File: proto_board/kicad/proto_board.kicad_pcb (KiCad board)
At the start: 2 copper layers, 91 x 96 mm, 1067 parts, among them J1 pcie_98

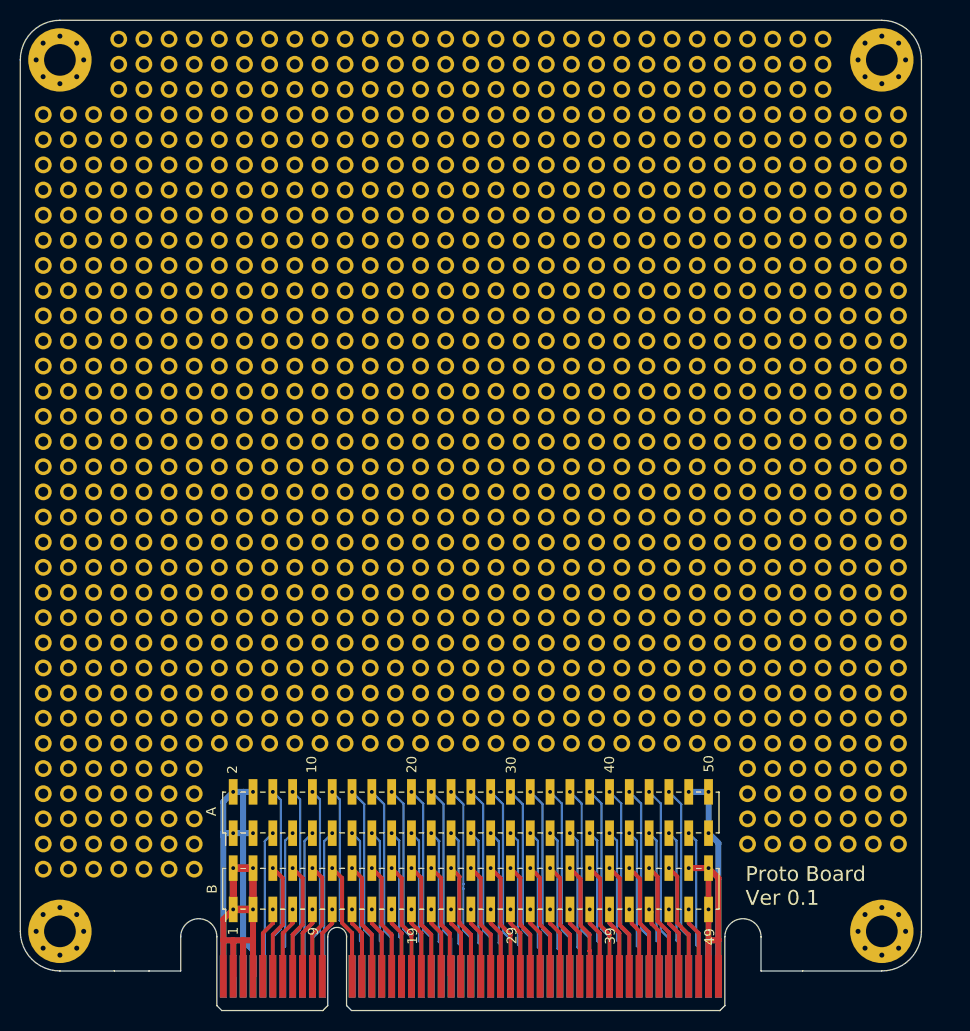
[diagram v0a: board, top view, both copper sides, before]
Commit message: Updated proto board to the common card outline.
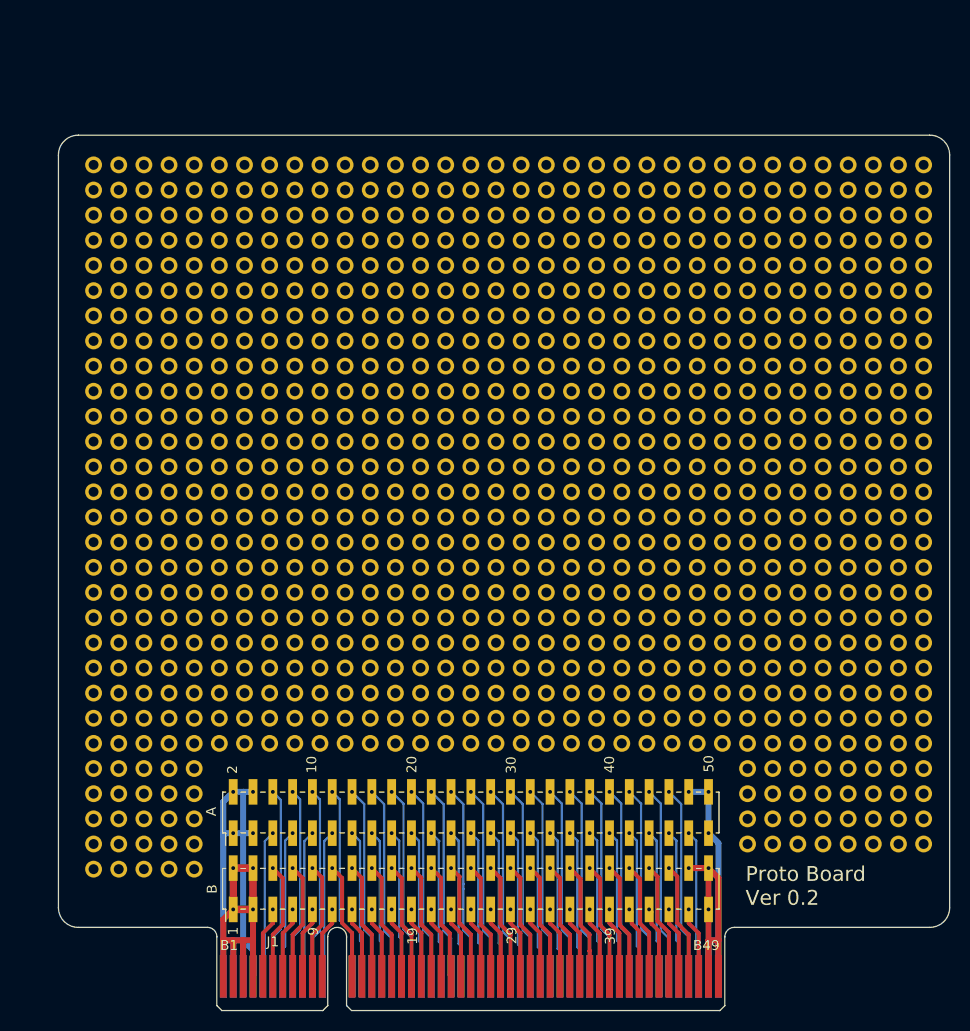
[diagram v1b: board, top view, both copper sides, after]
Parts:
- removed H1, H2, H3, H4: MountingHole, MountingHole:MountingHole_3.2mm_M3_Pad_Via
- removed the REF** at (51.6, -90.5)
- removed the REF** at (-14.4, -95.6)
- removed the REF** at (-14.4, -93.0)
- removed the REF** at (-27.1, -29.5)
- removed the REF** at (33.8, -93.0)
- removed the REF** at (21.1, -87.9)
- removed the REF** at (-27.1, -19.4)
- removed the REF** at (36.4, -90.5)
- removed the REF** at (-29.7, -21.9)
- removed the REF** at (-27.1, -37.1)
- removed the REF** at (5.88, -87.9)
- removed the REF** at (-27.1, -85.4)
- removed the REF** at (-24.6, -87.9)
- removed the REF** at (-29.7, -65.1)
- removed the REF** at (-27.1, -72.7)
- removed the REF** at (-27.1, -77.8)
- removed the REF** at (-29.7, -52.4)
- removed the REF** at (-14.4, -90.5)
- removed the REF** at (46.5, -95.6)
- removed the REF** at (13.5, -98.1)
- removed the REF** at (0.80, -90.5)
- removed the REF** at (49.1, -93.0)
- removed the REF** at (-17.0, -87.9)
- removed the REF** at (-22.1, -98.1)
- removed the REF** at (-29.7, -44.8)
- removed the REF** at (33.8, -90.5)
- removed the REF** at (3.34, -87.9)
- removed the REF** at (49.1, -95.6)
- removed the REF** at (44.0, -93.0)
- removed the REF** at (16.0, -93.0)
- removed the REF** at (-29.7, -14.3)
- removed the REF** at (-27.1, -57.5)
- removed the REF** at (11.0, -87.9)
- removed the REF** at (0.80, -98.1)
- removed the REF** at (-29.7, -60.0)
- removed the REF** at (36.4, -98.1)
- removed the REF** at (28.7, -93.0)
- removed the REF** at (-27.1, -39.7)
- removed the REF** at (-19.5, -98.1)
- removed the REF** at (36.4, -95.6)
- removed the REF** at (-29.7, -34.6)
- removed the REF** at (-9.36, -93.0)
- removed the REF** at (46.5, -87.9)
- removed the REF** at (21.1, -93.0)
- removed the REF** at (-6.82, -93.0)
- removed the REF** at (54.1, -90.5)
- removed the REF** at (11.0, -98.1)
- removed the REF** at (38.9, -95.6)
- removed the REF** at (8.42, -93.0)
- removed the REF** at (28.7, -95.6)
- removed the REF** at (-11.9, -98.1)
- removed the REF** at (38.9, -87.9)
- removed the REF** at (21.1, -98.1)
- removed the REF** at (-14.4, -98.1)
- removed the REF** at (18.6, -90.5)
- removed the REF** at (31.3, -87.9)
- removed the REF** at (-27.1, -24.4)
- removed the REF** at (26.2, -95.6)
- removed the REF** at (28.7, -87.9)
- removed the REF** at (-27.1, -44.8)
- removed the REF** at (0.80, -95.6)
- removed the REF** at (-22.1, -93.0)
- removed the REF** at (-17.0, -90.5)
- removed the REF** at (-29.7, -57.5)
- removed the REF** at (-29.7, -75.2)
- removed the REF** at (-1.74, -87.9)
- removed the REF** at (-29.7, -16.8)
- removed the REF** at (38.9, -93.0)
- removed the REF** at (49.1, -90.5)
- removed the REF** at (-19.5, -95.6)
- removed the REF** at (26.2, -90.5)
- removed the REF** at (-14.4, -87.9)
- removed the REF** at (8.42, -87.9)
- removed the REF** at (-9.36, -95.6)
- removed the REF** at (-27.1, -21.9)
- removed the REF** at (-29.7, -90.5)
- removed the REF** at (-27.1, -49.8)
- removed the REF** at (-27.1, -70.2)
- removed the REF** at (-27.1, -60.0)
- removed the REF** at (-29.7, -80.3)
- removed the REF** at (46.5, -90.5)
- removed the REF** at (33.8, -98.1)
- removed the REF** at (38.9, -98.1)
- removed the REF** at (-4.28, -95.6)
- removed the REF** at (-29.7, -24.4)
- removed the REF** at (16.0, -90.5)
- removed the REF** at (-29.7, -47.3)
- removed the REF** at (18.6, -93.0)
- removed the REF** at (0.80, -93.0)
- removed the REF** at (41.4, -98.1)
- removed the REF** at (8.42, -95.6)
- removed the REF** at (0.80, -87.9)
- removed the REF** at (-29.7, -49.8)
- removed the REF** at (-4.28, -93.0)
- removed the REF** at (5.88, -95.6)
- removed the REF** at (44.0, -90.5)
- removed the REF** at (41.4, -90.5)
- removed the REF** at (-29.7, -62.5)
- removed the REF** at (-17.0, -93.0)
- removed the REF** at (-29.7, -82.9)
- removed the REF** at (21.1, -95.6)
- removed the REF** at (13.5, -87.9)
- removed the REF** at (-27.1, -80.3)
- removed the REF** at (-22.1, -87.9)
- removed the REF** at (13.5, -90.5)
- removed the REF** at (16.0, -98.1)
- removed the REF** at (13.5, -95.6)
- removed the REF** at (-6.82, -87.9)
- removed the REF** at (-1.74, -95.6)
- removed the REF** at (51.6, -87.9)
- removed the REF** at (23.7, -98.1)
- removed the REF** at (23.7, -90.5)
- removed the REF** at (5.88, -90.5)
- removed the REF** at (23.7, -87.9)
- removed the REF** at (16.0, -95.6)
- removed the REF** at (-22.1, -90.5)
- removed the REF** at (-27.1, -87.9)
- removed the REF** at (13.5, -93.0)
- removed the REF** at (18.6, -95.6)
- removed the REF** at (-27.1, -82.9)
- removed the REF** at (-11.9, -87.9)
- removed the REF** at (-27.1, -47.3)
- removed the REF** at (-4.28, -90.5)
- removed the REF** at (49.1, -98.1)
- removed the REF** at (-27.1, -75.2)
- removed the REF** at (-6.82, -95.6)
- removed the REF** at (28.7, -90.5)
- removed the REF** at (44.0, -95.6)
- removed the REF** at (-1.74, -98.1)
- removed the REF** at (-6.82, -90.5)
- removed the REF** at (-29.7, -42.2)
- removed the REF** at (-29.7, -19.4)
- removed the REF** at (-9.36, -98.1)
- removed the REF** at (-27.1, -62.5)
- removed the REF** at (46.5, -98.1)
- removed the REF** at (-17.0, -98.1)
- removed the REF** at (41.4, -95.6)
- removed the REF** at (-11.9, -95.6)
- removed the REF** at (-29.7, -70.2)
- removed the REF** at (31.3, -93.0)
- removed the REF** at (-22.1, -95.6)
- removed the REF** at (41.4, -87.9)
- removed the REF** at (-9.36, -87.9)
- removed the REF** at (-27.1, -42.2)
- removed the REF** at (-4.28, -98.1)
- removed the REF** at (-1.74, -93.0)
- removed the REF** at (-27.1, -67.6)
- removed the REF** at (33.8, -87.9)
- removed the REF** at (18.6, -98.1)
- removed the REF** at (-27.1, -54.9)
- removed the REF** at (26.2, -98.1)
- removed the REF** at (36.4, -93.0)
- removed the REF** at (3.34, -95.6)
- removed the REF** at (56.7, -87.9)
- removed the REF** at (44.0, -87.9)
- removed the REF** at (44.0, -98.1)
- removed the REF** at (31.3, -95.6)
- removed the REF** at (56.7, -90.5)
- removed the REF** at (21.1, -90.5)
- removed the REF** at (16.0, -87.9)
- removed the REF** at (-17.0, -95.6)
- removed the REF** at (-29.7, -77.8)
- removed the REF** at (11.0, -93.0)
- removed the REF** at (11.0, -90.5)
- removed the REF** at (-11.9, -93.0)
- removed the REF** at (8.42, -98.1)
- removed the REF** at (54.1, -87.9)
- removed the REF** at (-27.1, -90.5)
- removed the REF** at (5.88, -98.1)
- removed the REF** at (41.4, -93.0)
- removed the REF** at (-29.7, -72.7)
- removed the REF** at (-6.82, -98.1)
- removed the REF** at (46.5, -93.0)
- removed the REF** at (-1.74, -90.5)
- removed the REF** at (-27.1, -14.3)
- removed the REF** at (-29.7, -37.1)
- removed the REF** at (-29.7, -39.7)
- removed the REF** at (11.0, -95.6)
- removed the REF** at (-29.7, -32.1)
- removed the REF** at (23.7, -93.0)
- removed the REF** at (28.7, -98.1)
- removed the REF** at (-29.7, -29.5)
- removed the REF** at (33.8, -95.6)
- removed the REF** at (-29.7, -67.6)
- removed the REF** at (5.88, -93.0)
- removed the REF** at (-27.1, -32.1)
- removed the REF** at (8.42, -90.5)
- removed the REF** at (38.9, -90.5)
- removed the REF** at (-27.1, -34.6)
- removed the REF** at (26.2, -87.9)
- removed the REF** at (-29.7, -87.9)
- removed the REF** at (-29.7, -54.9)
- removed the REF** at (26.2, -93.0)
- removed the REF** at (18.6, -87.9)
- removed the REF** at (-29.7, -85.4)
- removed the REF** at (-27.1, -27.0)
- removed the REF** at (-27.1, -65.1)
- removed the REF** at (31.3, -98.1)
- removed the REF** at (3.34, -90.5)
- removed the REF** at (-27.1, -52.4)
- removed the REF** at (-27.1, -16.8)
- removed the REF** at (-19.5, -93.0)
- removed the REF** at (49.1, -87.9)
- removed the REF** at (-19.5, -90.5)
- removed the REF** at (31.3, -90.5)
- removed the REF** at (23.7, -95.6)
- removed the REF** at (-11.9, -90.5)
- removed the REF** at (-29.7, -27.0)
- removed the REF** at (-24.6, -90.5)
- removed the REF** at (3.34, -93.0)
- removed the REF** at (36.4, -87.9)
- removed the REF** at (3.34, -98.1)
- removed the REF** at (-9.36, -90.5)
- removed the REF** at (-19.5, -87.9)
- removed the REF** at (-4.28, -87.9)
- added REF**: pad, proto_board:pad, F.Cu at (59.2, -32.1)
- added REF**: pad, proto_board:pad, F.Cu at (59.2, -82.9)
- added REF**: pad, proto_board:pad, F.Cu at (59.2, -16.8)
- added REF**: pad, proto_board:pad, F.Cu at (59.2, -67.6)
- added REF**: pad, proto_board:pad, F.Cu at (59.2, -65.1)
- added REF**: pad, proto_board:pad, F.Cu at (59.2, -57.5)
- added REF**: pad, proto_board:pad, F.Cu at (59.2, -54.9)
- added REF**: pad, proto_board:pad, F.Cu at (59.2, -52.4)
- added REF**: pad, proto_board:pad, F.Cu at (59.2, -44.8)
- added REF**: pad, proto_board:pad, F.Cu at (59.2, -19.4)
- added REF**: pad, proto_board:pad, F.Cu at (59.2, -70.2)
- added REF**: pad, proto_board:pad, F.Cu at (59.2, -29.5)
- added REF**: pad, proto_board:pad, F.Cu at (59.2, -21.9)
- added REF**: pad, proto_board:pad, F.Cu at (59.2, -42.2)
- added REF**: pad, proto_board:pad, F.Cu at (59.2, -85.4)
- added REF**: pad, proto_board:pad, F.Cu at (59.2, -49.8)
- added REF**: pad, proto_board:pad, F.Cu at (59.2, -37.1)
- added REF**: pad, proto_board:pad, F.Cu at (59.2, -39.7)
- added REF**: pad, proto_board:pad, F.Cu at (59.2, -27.0)
- added REF**: pad, proto_board:pad, F.Cu at (59.2, -60.0)
- added REF**: pad, proto_board:pad, F.Cu at (59.2, -47.3)
- added REF**: pad, proto_board:pad, F.Cu at (59.2, -24.4)
- added REF**: pad, proto_board:pad, F.Cu at (59.2, -62.5)
- added REF**: pad, proto_board:pad, F.Cu at (59.2, -72.7)
- added REF**: pad, proto_board:pad, F.Cu at (59.2, -34.6)
- added REF**: pad, proto_board:pad, F.Cu at (59.2, -80.3)
- added REF**: pad, proto_board:pad, F.Cu at (59.2, -75.2)
- added REF**: pad, proto_board:pad, F.Cu at (59.2, -77.8)
- J1: footprint proto_board:pcie_98_edge -> common:PCIE_98_CARD
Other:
- board size 91 x 96 mm -> 90 x 88.4 mm
- board text added: "Proto Board Ver 0.2"
- board text removed: "49"
- board text removed: "Proto Board Ver 0.1"
